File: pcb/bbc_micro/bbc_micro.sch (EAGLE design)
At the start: 51 parts, among them IC1 STM32F072C8T6, SW1 324_SW, SW2 324_SW, SW3 324_SW

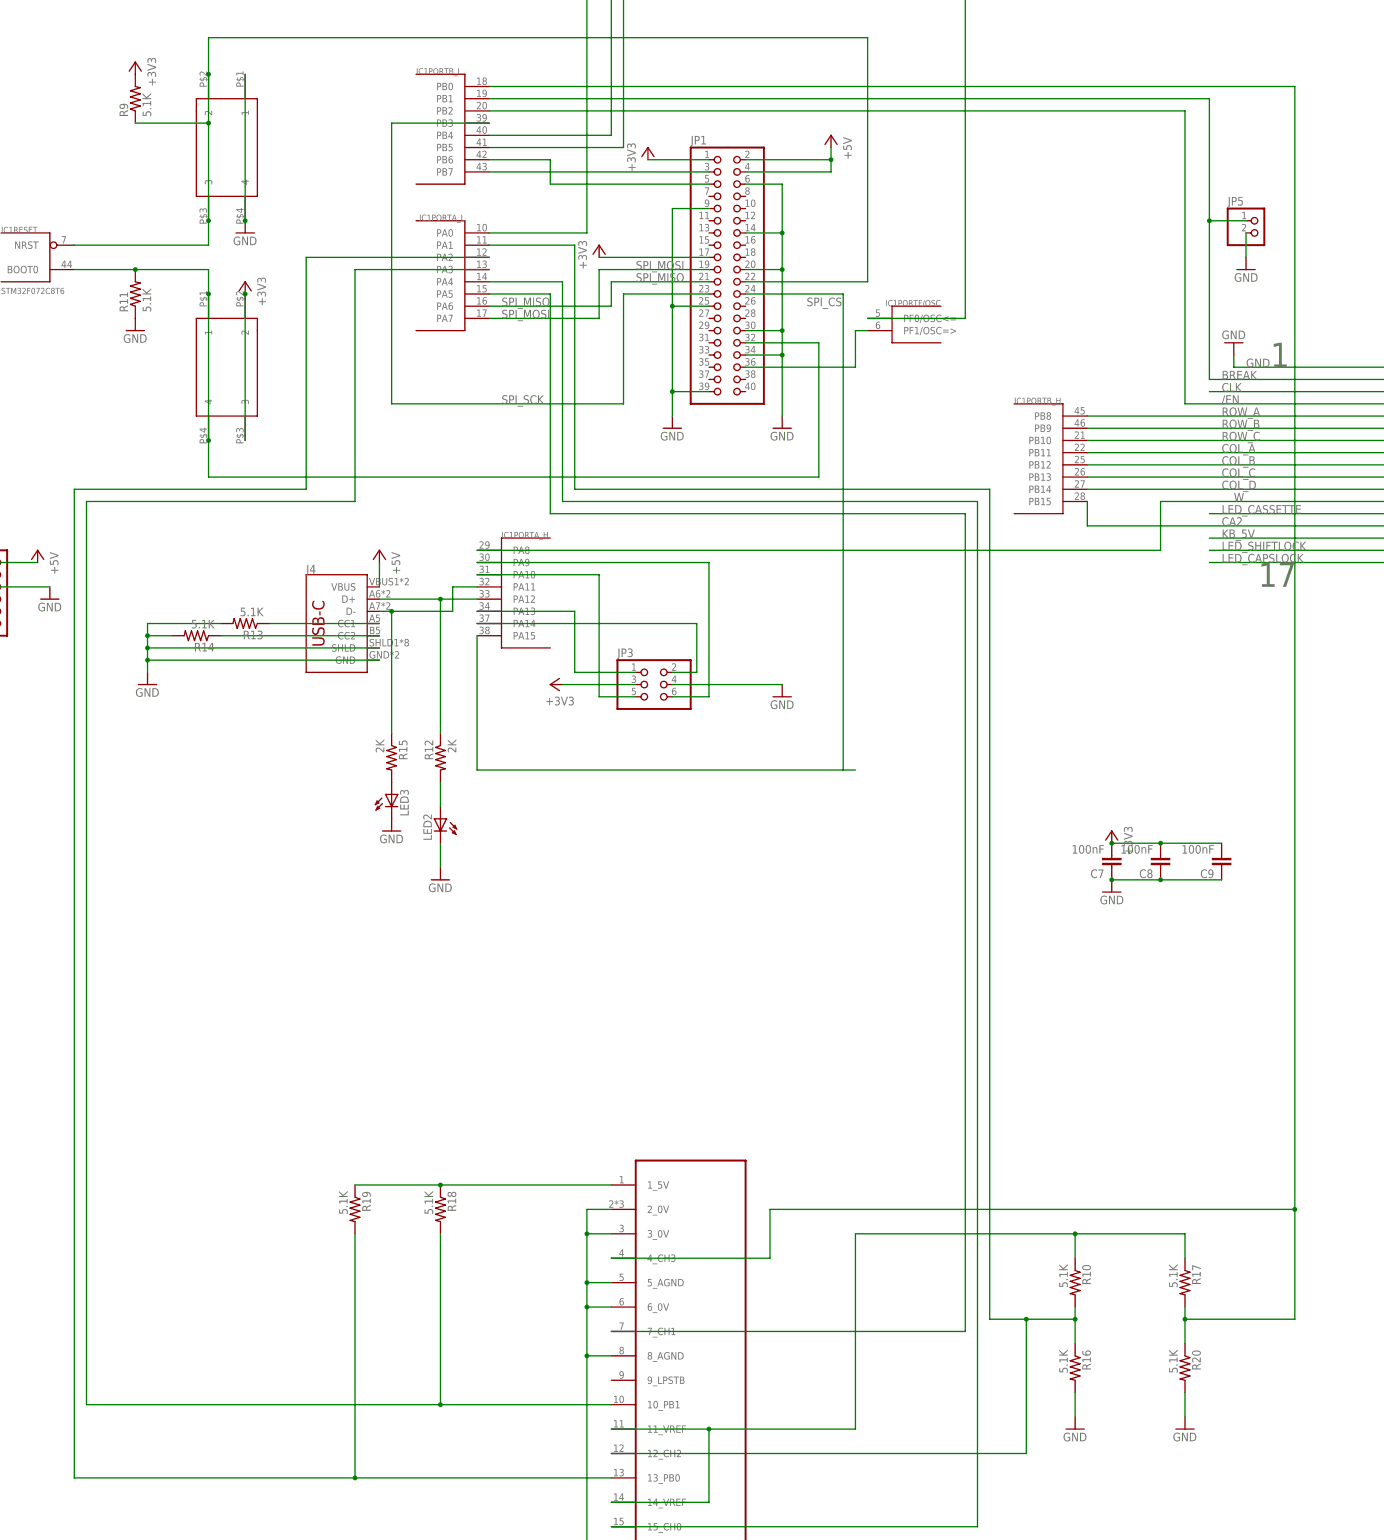
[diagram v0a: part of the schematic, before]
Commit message: removed second joystick and added BBC VREF input
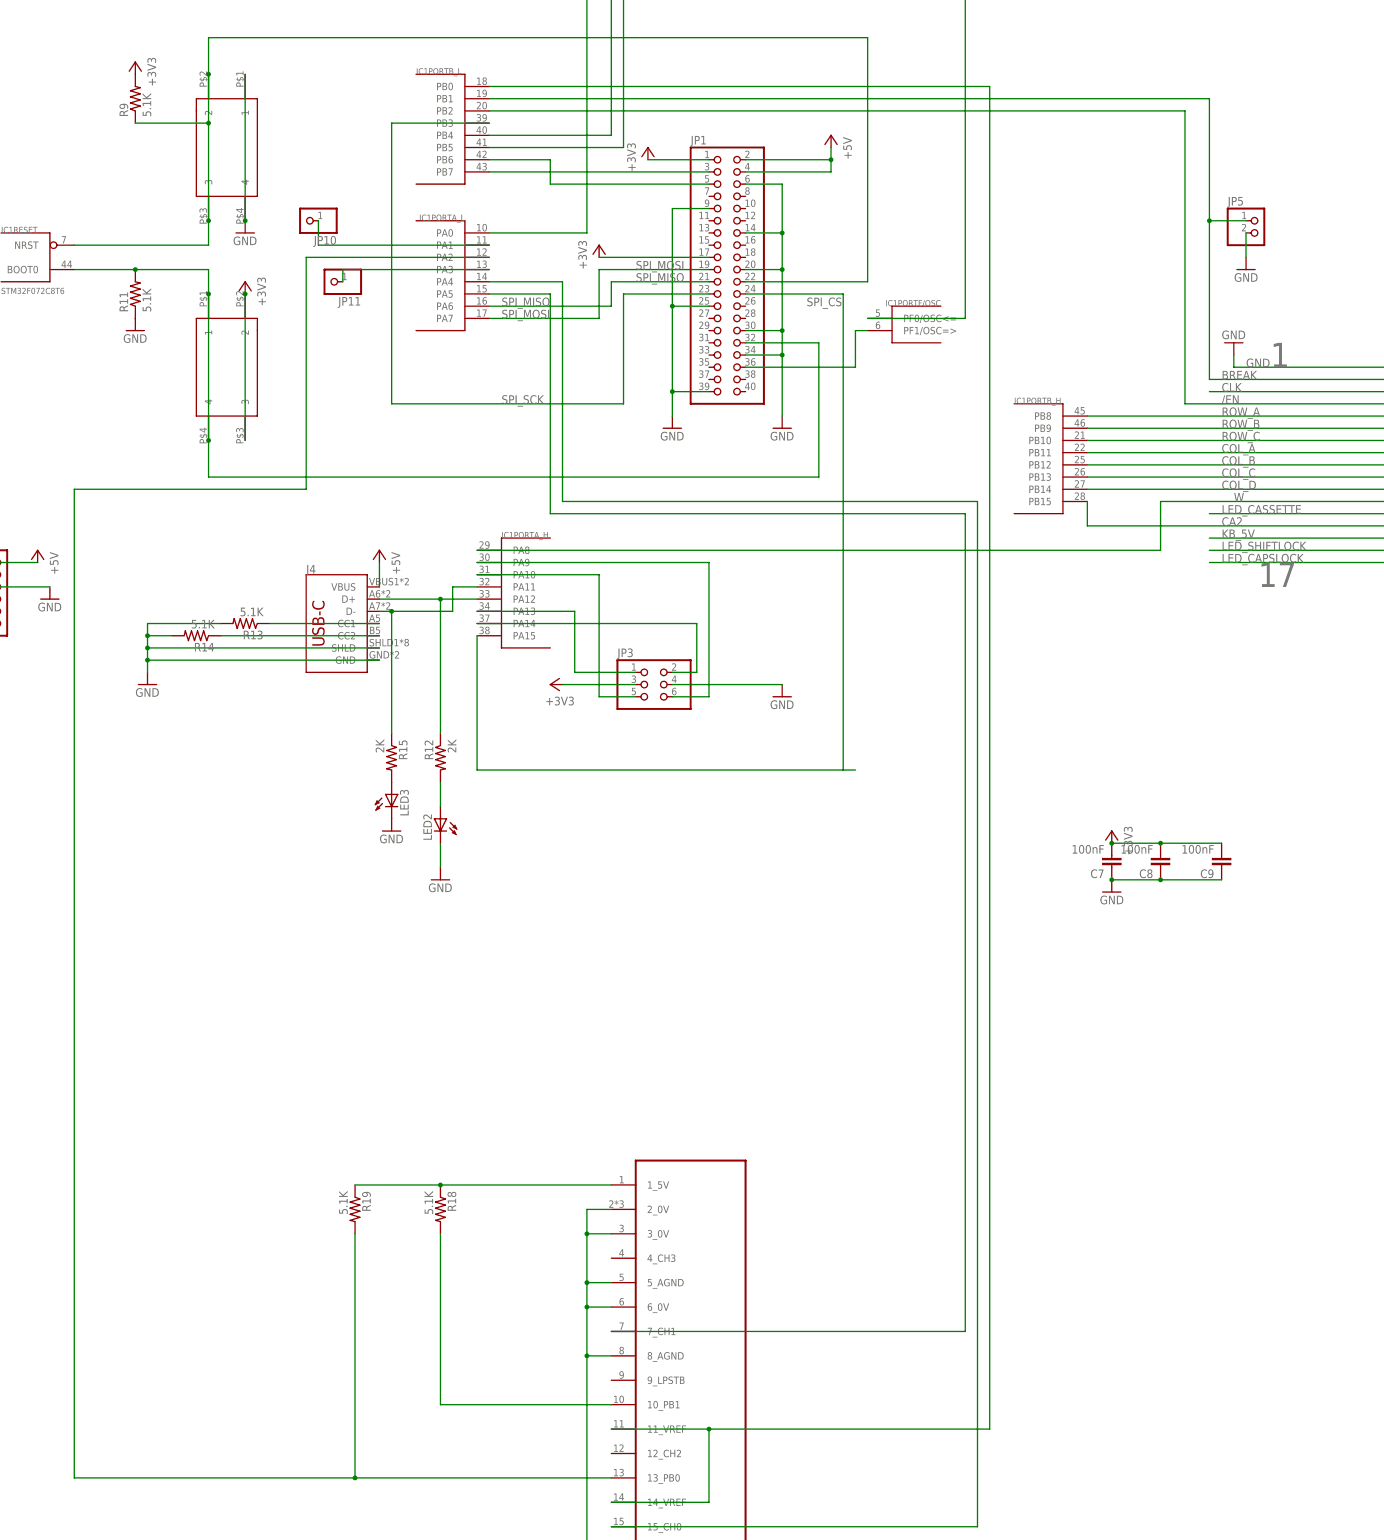
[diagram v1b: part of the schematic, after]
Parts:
- removed R10, R16, R17, R20: 5.1K, SparkFun-Passives:RESISTOR0805-RES
- added JP10, JP11: (no value), adafruit_changed:PINHD-1X1CB
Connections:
- removed net N$17: IC1PORTA_L.PA1, R10.2, R16.1, U$9.12_CH2
- new net N$11: IC1PORTA_L.PA1, JP10.1
- net GND: no longer R16.2, R20.2
- net N$10: now also IC1PORTB_L.PB0; no longer R10.1, R17.1
- net N$12: now also IC1PORTA_L.PA3, JP11.1; no longer IC1PORTB_L.PB0, R17.2, R20.1, U$9.4_CH3
- net N$21: no longer IC1PORTA_L.PA3
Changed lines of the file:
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@@
 <part name="R24" library="SparkFun-Passives" deviceset="RESISTOR" device="0805-RES" value="2K"/>
 <part name="R25" library="SparkFun-Passives" deviceset="RESISTOR" device="0805-RES" value="2K"/>
-<part name="R10" library="SparkFun-Passives" deviceset="RESISTOR" device="0805-RES" value="5.1K"/>
-<part name="R16" library="SparkFun-Passives" deviceset="RESISTOR" device="0805-RES" value="5.1K"/>
-<part name="R17" library="SparkFun-Passives" deviceset="RESISTOR" device="0805-RES" value="5.1K"/>
-<part name="R20" library="SparkFun-Passives" deviceset="RESISTOR" device="0805-RES" value="5.1K"/>
-<part name="GND11" library="supply1" library_urn="urn:adsk.eagle:library:371" deviceset="GND" device=""/>
-<part name="GND14" library="supply1" library_urn="urn:adsk.eagle:library:371" deviceset="GND" device=""/>
 <part name="R26" library="SparkFun-Passives" deviceset="RESISTOR" device="0805-RES" value="5.1K"/>
 <part name="GND16" library="supply1" library_urn="urn:adsk.eagle:library:371" deviceset="GND" device=""/>
 <part name="JP5" library="pinhead" library_urn="urn:adsk.eagle:library:325" deviceset="PINHD-1X2" device="" package3d_urn="urn:adsk.eagle:package:22435/2"/>
 <part name="GND19" library="supply1" deviceset="GND" device=""/>
+<part name="JP10" library="adafruit_changed" deviceset="PINHD-1X1" device="CB"/>
+<part name="JP11" library="adafruit_changed" deviceset="PINHD-1X1" device="CB"/>
 </parts>
 <sheets>
@@
 <attribute name="VALUE" x="276.098" y="-34.29" size="1.778" layer="96" rot="R270"/>
 </instance>
-<instance part="R10" gate="G$1" x="165.1" y="-190.5" smashed="yes" rot="R270">
-<attribute name="NAME" x="166.5986" y="-186.69" size="1.778" layer="95" rot="R270"/>
-<attribute name="VALUE" x="161.798" y="-186.69" size="1.778" layer="96" rot="R270"/>
-</instance>
-<instance part="R16" gate="G$1" x="165.1" y="-208.28" smashed="yes" rot="R270">
-<attribute name="NAME" x="166.5986" y="-204.47" size="1.778" layer="95" rot="R270"/>
-<attribute name="VALUE" x="161.798" y="-204.47" size="1.778" layer="96" rot="R270"/>
-</instance>
-<instance part="R17" gate="G$1" x="187.96" y="-190.5" smashed="yes" rot="R270">
-<attribute name="NAME" x="189.4586" y="-186.69" size="1.778" layer="95" rot="R270"/>
-<attribute name="VALUE" x="184.658" y="-186.69" size="1.778" layer="96" rot="R270"/>
-</instance>
-<instance part="R20" gate="G$1" x="187.96" y="-208.28" smashed="yes" rot="R270">
-<attribute name="NAME" x="189.4586" y="-204.47" size="1.778" layer="95" rot="R270"/>
-<attribute name="VALUE" x="184.658" y="-204.47" size="1.778" layer="96" rot="R270"/>
-</instance>
-<instance part="GND11" gate="1" x="165.1" y="-220.98" smashed="yes">
-<attribute name="VALUE" x="162.56" y="-223.52" size="1.778" layer="96"/>
-</instance>
-<instance part="GND14" gate="1" x="187.96" y="-220.98" smashed="yes">
-<attribute name="VALUE" x="185.42" y="-223.52" size="1.778" layer="96"/>
-</instance>
 <instance part="R26" gate="G$1" x="274.32" y="-10.16" smashed="yes" rot="R270">
 <attribute name="NAME" x="275.8186" y="-6.35" size="1.778" layer="95" rot="R270"/>
@@
 <instance part="GND19" gate="1" x="200.66" y="20.32" smashed="yes" rot="MR0">
 <attribute name="VALUE" x="203.2" y="17.78" size="1.778" layer="96" rot="MR0"/>
+</instance>
+<instance part="JP10" gate="G$1" x="5.08" y="30.48" smashed="yes" rot="R180">
+<attribute name="NAME" x="11.43" y="27.305" size="1.778" layer="95" rot="R180"/>
+<attribute name="VALUE" x="11.43" y="35.56" size="1.778" layer="96" rot="R180"/>
+</instance>
+<instance part="JP11" gate="G$1" x="10.16" y="17.78" smashed="yes" rot="R180">
+<attribute name="NAME" x="16.51" y="14.605" size="1.778" layer="95" rot="R180"/>
+<attribute name="VALUE" x="16.51" y="22.86" size="1.778" layer="96" rot="R180"/>
 </instance>
 </instances>
@@
 </segment>
 <segment>
-<pinref part="R16" gate="G$1" pin="2"/>
-<pinref part="GND11" gate="1" pin="GND"/>
-<wire x1="165.1" y1="-213.36" x2="165.1" y2="-218.44" width="0.1524" layer="91"/>
-</segment>
-<segment>
-<pinref part="R20" gate="G$1" pin="2"/>
-<pinref part="GND14" gate="1" pin="GND"/>
-<wire x1="187.96" y1="-213.36" x2="187.96" y2="-218.44" width="0.1524" layer="91"/>
-</segment>
-<segment>
 <pinref part="R26" gate="G$1" pin="2"/>
 <pinref part="GND16" gate="1" pin="GND"/>
@@
 <wire x1="22.86" y1="-50.8" x2="22.86" y2="-76.2" width="0.1524" layer="91"/>
 <junction x="22.86" y="-50.8"/>
-</segment>
-</net>
-<net name="N$12" class="0">
-<segment>
-<pinref part="R17" gate="G$1" pin="2"/>
-<pinref part="R20" gate="G$1" pin="1"/>
-<wire x1="187.96" y1="-195.58" x2="187.96" y2="-198.12" width="0.1524" layer="91"/>
-<wire x1="187.96" y1="-198.12" x2="187.96" y2="-203.2" width="0.1524" layer="91"/>
-<wire x1="187.96" y1="-198.12" x2="210.82" y2="-198.12" width="0.1524" layer="91"/>
-<wire x1="210.82" y1="-198.12" x2="210.82" y2="-175.26" width="0.1524" layer="91"/>
-<junction x="187.96" y="-198.12"/>
-<wire x1="210.82" y1="-175.26" x2="101.6" y2="-175.26" width="0.1524" layer="91"/>
-<wire x1="101.6" y1="-175.26" x2="101.6" y2="-185.42" width="0.1524" layer="91"/>
-<pinref part="U$9" gate="G$1" pin="4_CH3"/>
-<wire x1="101.6" y1="-185.42" x2="68.58" y2="-185.42" width="0.1524" layer="91"/>
-<wire x1="210.82" y1="58.42" x2="210.82" y2="-175.26" width="0.1524" layer="91"/>
-<junction x="210.82" y="-175.26"/>
-<pinref part="IC1" gate="PORTB_L" pin="PB0"/>
-<wire x1="210.82" y1="58.42" x2="43.18" y2="58.42" width="0.1524" layer="91"/>
 </segment>
 </net>
@@
 <wire x1="33.02" y1="-180.34" x2="33.02" y2="-215.9" width="0.1524" layer="91"/>
 <wire x1="33.02" y1="-215.9" x2="68.58" y2="-215.9" width="0.1524" layer="91"/>
-<pinref part="IC1" gate="PORTA_L" pin="PA3"/>
-<wire x1="43.18" y1="20.32" x2="15.24" y2="20.32" width="0.1524" layer="91"/>
-<wire x1="15.24" y1="20.32" x2="15.24" y2="-27.94" width="0.1524" layer="91"/>
-<wire x1="15.24" y1="-27.94" x2="-40.64" y2="-27.94" width="0.1524" layer="91"/>
-<wire x1="-40.64" y1="-27.94" x2="-40.64" y2="-215.9" width="0.1524" layer="91"/>
-<wire x1="33.02" y1="-215.9" x2="-40.64" y2="-215.9" width="0.1524" layer="91"/>
-<junction x="33.02" y="-215.9"/>
 </segment>
 </net>
@@
 </segment>
 </net>
-<net name="N$17" class="0">
-<segment>
-<pinref part="IC1" gate="PORTA_L" pin="PA1"/>
-<wire x1="43.18" y1="25.4" x2="60.96" y2="25.4" width="0.1524" layer="91"/>
-<wire x1="60.96" y1="25.4" x2="60.96" y2="-25.4" width="0.1524" layer="91"/>
-<wire x1="60.96" y1="-25.4" x2="147.32" y2="-25.4" width="0.1524" layer="91"/>
-<pinref part="R10" gate="G$1" pin="2"/>
-<pinref part="R16" gate="G$1" pin="1"/>
-<wire x1="165.1" y1="-195.58" x2="165.1" y2="-198.12" width="0.1524" layer="91"/>
-<wire x1="165.1" y1="-198.12" x2="165.1" y2="-203.2" width="0.1524" layer="91"/>
-<wire x1="165.1" y1="-198.12" x2="154.94" y2="-198.12" width="0.1524" layer="91"/>
-<wire x1="154.94" y1="-198.12" x2="154.94" y2="-226.06" width="0.1524" layer="91"/>
-<junction x="165.1" y="-198.12"/>
-<pinref part="U$9" gate="G$1" pin="12_CH2"/>
-<wire x1="154.94" y1="-226.06" x2="68.58" y2="-226.06" width="0.1524" layer="91"/>
-<wire x1="147.32" y1="-25.4" x2="147.32" y2="-198.12" width="0.1524" layer="91"/>
-<wire x1="147.32" y1="-198.12" x2="154.94" y2="-198.12" width="0.1524" layer="91"/>
-<junction x="154.94" y="-198.12"/>
-</segment>
-</net>
 <net name="N$6" class="0">
 <segment>
@@
 <wire x1="88.9" y1="-220.98" x2="88.9" y2="-236.22" width="0.1524" layer="91"/>
 <junction x="88.9" y="-220.98"/>
-<wire x1="88.9" y1="-220.98" x2="119.38" y2="-220.98" width="0.1524" layer="91"/>
-<wire x1="119.38" y1="-220.98" x2="119.38" y2="-180.34" width="0.1524" layer="91"/>
-<pinref part="R10" gate="G$1" pin="1"/>
-<wire x1="165.1" y1="-180.34" x2="165.1" y2="-185.42" width="0.1524" layer="91"/>
-<wire x1="165.1" y1="-180.34" x2="119.38" y2="-180.34" width="0.1524" layer="91"/>
-<junction x="165.1" y="-180.34"/>
-<wire x1="187.96" y1="-180.34" x2="165.1" y2="-180.34" width="0.1524" layer="91"/>
-<pinref part="R17" gate="G$1" pin="1"/>
-<wire x1="187.96" y1="-185.42" x2="187.96" y2="-180.34" width="0.1524" layer="91"/>
-</segment>
-</net>
+<wire x1="88.9" y1="-220.98" x2="147.32" y2="-220.98" width="0.1524" layer="91"/>
+<pinref part="IC1" gate="PORTB_L" pin="PB0"/>
+<wire x1="43.18" y1="58.42" x2="147.32" y2="58.42" width="0.1524" layer="91"/>
+<wire x1="147.32" y1="58.42" x2="147.32" y2="-220.98" width="0.1524" layer="91"/>
+</segment>
+</net>
+<net name="N$11" class="0">
+<segment>
+<pinref part="IC1" gate="PORTA_L" pin="PA1"/>
+<pinref part="JP10" gate="G$1" pin="1"/>
+<wire x1="43.18" y1="25.4" x2="7.62" y2="25.4" width="0.1524" layer="91"/>
+<wire x1="7.62" y1="25.4" x2="7.62" y2="30.48" width="0.1524" layer="91"/>
+</segment>
+</net>
+<net name="N$12" class="0">
+<segment>
+<pinref part="IC1" gate="PORTA_L" pin="PA3"/>
+<pinref part="JP11" gate="G$1" pin="1"/>
+<wire x1="43.18" y1="20.32" x2="12.7" y2="20.32" width="0.1524" layer="91"/>
+<wire x1="12.7" y1="20.32" x2="12.7" y2="17.78" width="0.1524" layer="91"/>
+</segment>
+</net>

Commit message: added a pot, clean up
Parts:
- added R10: (no value), SparkFun-Retired:TRIMPOTPTH
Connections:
- net +3V3: now also R10.CW
- net GND: now also R10.CCW
- net N$12: now also R10.WIPER
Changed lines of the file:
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@@
 <part name="JP10" library="adafruit_changed" deviceset="PINHD-1X1" device="CB"/>
 <part name="JP11" library="adafruit_changed" deviceset="PINHD-1X1" device="CB"/>
+<part name="R10" library="SparkFun-Retired" deviceset="TRIMPOT" device="PTH"/>
+<part name="+3V7" library="backplane" deviceset="+3V3" device=""/>
+<part name="GND11" library="supply1" library_urn="urn:adsk.eagle:library:371" deviceset="GND" device=""/>
 </parts>
 <sheets>
@@
 <attribute name="VALUE" x="16.51" y="22.86" size="1.778" layer="96" rot="R180"/>
 </instance>
+<instance part="R10" gate="R?" x="12.7" y="2.54" smashed="yes">
+<attribute name="NAME" x="1.27" y="4.0386" size="1.778" layer="95"/>
+<attribute name="VALUE" x="8.89" y="-0.762" size="1.778" layer="96"/>
+</instance>
+<instance part="+3V7" gate="G$1" x="17.78" y="5.08" smashed="yes" rot="MR0">
+<attribute name="VALUE" x="20.32" y="0" size="1.778" layer="96" rot="MR90"/>
+</instance>
+<instance part="GND11" gate="1" x="7.62" y="0" smashed="yes">
+<attribute name="VALUE" x="5.08" y="-2.54" size="1.778" layer="96"/>
+</instance>
 </instances>
 <busses>
@@
 <wire x1="-60.96" y1="-53.34" x2="-60.96" y2="-50.8" width="0.1524" layer="91"/>
 <junction x="-60.96" y="-50.8"/>
+</segment>
+<segment>
+<pinref part="R10" gate="R?" pin="CW"/>
+<pinref part="+3V7" gate="G$1" pin="+3V3"/>
 </segment>
 </net>
@@
 <wire x1="200.66" y1="27.94" x2="200.66" y2="22.86" width="0.1524" layer="91"/>
 </segment>
+<segment>
+<pinref part="R10" gate="R?" pin="CCW"/>
+<pinref part="GND11" gate="1" pin="GND"/>
+</segment>
 </net>
 <net name="N$29" class="0">
@@
 <wire x1="43.18" y1="20.32" x2="12.7" y2="20.32" width="0.1524" layer="91"/>
 <wire x1="12.7" y1="20.32" x2="12.7" y2="17.78" width="0.1524" layer="91"/>
-</segment>
-</net>
+<pinref part="R10" gate="R?" pin="WIPER"/>
+<wire x1="12.7" y1="17.78" x2="12.7" y2="7.62" width="0.1524" layer="91"/>
+<junction x="12.7" y="17.78"/>
+</segment>
+</net>
